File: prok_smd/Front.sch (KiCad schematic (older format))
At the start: 31 parts, among them CON1 microSD_Card, J12 Conn_01x05_Male, J13 Conn_01x04_Male, J14 Conn_01x04_Male, J5 TIME_CV, J6 CHANNEL_CV, J7 RESET_CV, J8 OUT, SW1 KS01BL

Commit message: :construction: Locked headers and added mousebites
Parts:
- removed J13, J14: Conn_01x04_Male, Connector_PinHeader_2.54mm:PinHeader_1x04_P2.54mm_Vertical, symbol Connector:Conn_01x04_Male
- added J15, J16, J17, J18: Conn_01x02_Male, Connector_PinHeader_2.54mm:PinHeader_1x02_P2.54mm_Vertical, symbol Connector:Conn_01x02_Male
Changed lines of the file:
@@
 L power:-12V #PWR?
 U 1 1 5D1D35EB
-P 2650 7050
+P 2650 7250
 AR Path="/5D1D35EB" Ref="#PWR?"  Part="1"
 AR Path="/5D2626DC/5D1D35EB" Ref="#PWR0142"  Part="1"
-F 0 "#PWR0142" H 2650 7150 50  0001 C CNN
-F 1 "-12V" H 2665 7223 50  0000 C CNN
-F 2 "" H 2650 7050 50  0001 C CNN
-F 3 "" H 2650 7050 50  0001 C CNN
-	1    2650 7050
+F 0 "#PWR0142" H 2650 7350 50  0001 C CNN
+F 1 "-12V" H 2665 7423 50  0000 C CNN
+F 2 "" H 2650 7250 50  0001 C CNN
+F 3 "" H 2650 7250 50  0001 C CNN
+	1    2650 7250
 	0    -1   -1   0
 $EndComp
@@
 L power:+5V #PWR?
 U 1 1 5D1D35FD
-P 2650 7250
+P 2650 7050
 AR Path="/5D1D35FD" Ref="#PWR?"  Part="1"
 AR Path="/5D2626DC/5D1D35FD" Ref="#PWR0145"  Part="1"
-F 0 "#PWR0145" H 2650 7100 50  0001 C CNN
-F 1 "+5V" V 2665 7378 50  0000 L CNN
-F 2 "" H 2650 7250 50  0001 C CNN
-F 3 "" H 2650 7250 50  0001 C CNN
-	1    2650 7250
+F 0 "#PWR0145" H 2650 6900 50  0001 C CNN
+F 1 "+5V" V 2665 7178 50  0000 L CNN
+F 2 "" H 2650 7050 50  0001 C CNN
+F 3 "" H 2650 7050 50  0001 C CNN
+	1    2650 7050
 	0    -1   -1   0
 $EndComp
@@
 	2650 7250 2750 7250
 $Comp
-L Connector:Conn_01x04_Male J13
-U 1 1 5D1D4B46
-P 4050 7050
-F 0 "J13" H 4156 7328 50  0000 C CNN
-F 1 "Conn_01x04_Male" H 4156 7237 50  0000 C CNN
-F 2 "Connector_PinHeader_2.54mm:PinHeader_1x04_P2.54mm_Vertical" H 4050 7050 50  0001 C CNN
-F 3 "~" H 4050 7050 50  0001 C CNN
-	1    4050 7050
-	1    0    0    -1
-$EndComp
-$Comp
-L Connector:Conn_01x04_Male J14
-U 1 1 5D1D4BBA
-P 4650 7150
-F 0 "J14" H 4623 7030 50  0000 R CNN
-F 1 "Conn_01x04_Male" H 4623 7121 50  0000 R CNN
-F 2 "Connector_PinHeader_2.54mm:PinHeader_1x04_P2.54mm_Vertical" H 4650 7150 50  0001 C CNN
-F 3 "~" H 4650 7150 50  0001 C CNN
-	1    4650 7150
-	-1   0    0    1
-$EndComp
-$Comp
 L Connector:Conn_01x05_Male J12
 U 1 1 5D1DA55A
@@
 	-1   0    0    -1
 $EndComp
+$Comp
+L Connector:Conn_01x02_Male J15
+U 1 1 5D21284E
+P 4050 6950
+F 0 "J15" H 4156 7128 50  0000 C CNN
+F 1 "Conn_01x02_Male" H 4156 7037 50  0000 C CNN
+F 2 "Connector_PinHeader_2.54mm:PinHeader_1x02_P2.54mm_Vertical" H 4050 6950 50  0001 C CNN
+F 3 "~" H 4050 6950 50  0001 C CNN
+	1    4050 6950
+	1    0    0    -1
+$EndComp
+$Comp
+L Connector:Conn_01x02_Male J16
+U 1 1 5D2128C0
+P 4050 7150
+F 0 "J16" H 4156 7328 50  0000 C CNN
+F 1 "Conn_01x02_Male" H 4156 7237 50  0000 C CNN
+F 2 "Connector_PinHeader_2.54mm:PinHeader_1x02_P2.54mm_Vertical" H 4050 7150 50  0001 C CNN
+F 3 "~" H 4050 7150 50  0001 C CNN
+	1    4050 7150
+	1    0    0    -1
+$EndComp
+$Comp
+L Connector:Conn_01x02_Male J17
+U 1 1 5D212916
+P 4650 7050
+F 0 "J17" H 4623 6930 50  0000 R CNN
+F 1 "Conn_01x02_Male" H 4623 7021 50  0000 R CNN
+F 2 "Connector_PinHeader_2.54mm:PinHeader_1x02_P2.54mm_Vertical" H 4650 7050 50  0001 C CNN
+F 3 "~" H 4650 7050 50  0001 C CNN
+	1    4650 7050
+	-1   0    0    1
+$EndComp
+$Comp
+L Connector:Conn_01x02_Male J18
+U 1 1 5D2129C8
+P 4650 7250
+F 0 "J18" H 4623 7130 50  0000 R CNN
+F 1 "Conn_01x02_Male" H 4623 7221 50  0000 R CNN
+F 2 "Connector_PinHeader_2.54mm:PinHeader_1x02_P2.54mm_Vertical" H 4650 7250 50  0001 C CNN
+F 3 "~" H 4650 7250 50  0001 C CNN
+	1    4650 7250
+	-1   0    0    1
+$EndComp
 $EndSCHEMATC

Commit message: :construction: first draft routing
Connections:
- wire segments 64 -> 68
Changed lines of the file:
@@
 	4350 7250 4450 7250
-Wire Wire Line
-	4450 7150 4250 7150
-Wire Wire Line
-	4250 7050 4450 7050
 Wire Wire Line
 	4450 6950 4350 6950
 Wire Wire Line
-	4350 6950 4350 7250
+	4350 6950 4350 7050
 Connection ~ 4350 6950
 Wire Wire Line
@@
 	-1   0    0    1
 $EndComp
+Wire Wire Line
+	4250 7050 4350 7050
+Connection ~ 4350 7050
+Wire Wire Line
+	4350 7050 4350 7150
+Wire Wire Line
+	4350 7050 4450 7050
+Wire Wire Line
+	4250 7150 4350 7150
+Connection ~ 4350 7150
+Wire Wire Line
+	4350 7150 4350 7250
+Wire Wire Line
+	4350 7150 4450 7150
 $EndSCHEMATC

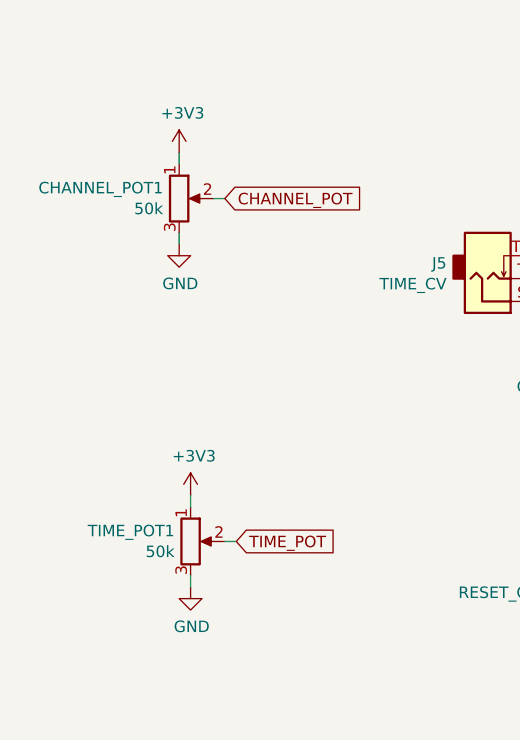
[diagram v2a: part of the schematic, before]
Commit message: :bug: fixed backwards pots
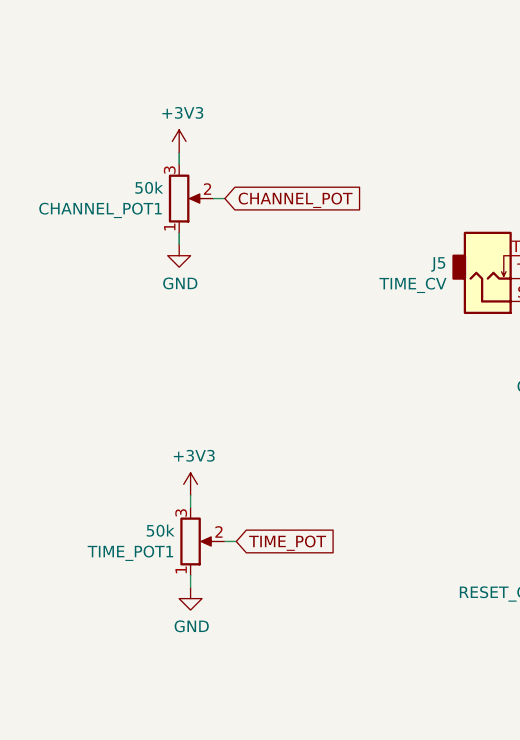
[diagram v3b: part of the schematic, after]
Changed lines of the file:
@@
 F 3 "~" H 1350 2750 50  0001 C CNN
 	1    1350 2750
-	1    0    0    -1
+	1    0    0    1
 $EndComp
 $Comp
@@
 F 3 "~" H 1400 4250 50  0001 C CNN
 	1    1400 4250
-	1    0    0    -1
+	1    0    0    1
 $EndComp
 $Comp

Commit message: :sparkles: Fixed switch led
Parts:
- removed D9: LED, symbol Device:LED
- removed SW1: KS01BL, prok_smd:KS01BL, symbol Switch:SW_SPST
- added SW1: SW_Push_LED, prok_smd:KS01BL, symbol Switch:SW_Push_LED
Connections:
- wire segments 68 -> 66
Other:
- moved on the sheet: R12
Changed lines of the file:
@@
 L Device:R R12
 U 1 1 5D27E545
-P 5550 1450
-F 0 "R12" H 5620 1496 50  0000 L CNN
-F 1 "27k" H 5620 1405 50  0000 L CNN
-F 2 "Resistor_SMD:R_0603_1608Metric" V 5480 1450 50  0001 C CNN
-F 3 "~" H 5550 1450 50  0001 C CNN
-	1    5550 1450
+P 5600 1900
+F 0 "R12" H 5670 1946 50  0000 L CNN
+F 1 "27k" H 5670 1855 50  0000 L CNN
+F 2 "Resistor_SMD:R_0603_1608Metric" V 5530 1900 50  0001 C CNN
+F 3 "~" H 5600 1900 50  0001 C CNN
+	1    5600 1900
 	1    0    0    -1
 $EndComp
@@
 L power:GND #PWR0126
 U 1 1 5D280887
-P 5550 1650
-F 0 "#PWR0126" H 5550 1400 50  0001 C CNN
-F 1 "GND" H 5555 1477 50  0000 C CNN
-F 2 "" H 5550 1650 50  0001 C CNN
-F 3 "" H 5550 1650 50  0001 C CNN
-	1    5550 1650
-	1    0    0    -1
-$EndComp
-Wire Wire Line
-	5550 1650 5550 1600
-Wire Wire Line
-	5550 1300 6000 1300
-$Comp
-L Switch:SW_SPST SW1
-U 1 1 5D280CD0
-P 5200 1300
-F 0 "SW1" H 5200 1535 50  0000 C CNN
-F 1 "KS01BL" H 5200 1444 50  0000 C CNN
-F 2 "prok_smd:KS01BL" H 5200 1300 50  0001 C CNN
-F 3 "" H 5200 1300 50  0001 C CNN
-	1    5200 1300
-	1    0    0    -1
-$EndComp
-Wire Wire Line
-	5400 1300 5550 1300
-Connection ~ 5550 1300
+P 5600 2100
+F 0 "#PWR0126" H 5600 1850 50  0001 C CNN
+F 1 "GND" H 5605 1927 50  0000 C CNN
+F 2 "" H 5600 2100 50  0001 C CNN
+F 3 "" H 5600 2100 50  0001 C CNN
+	1    5600 2100
+	1    0    0    -1
+$EndComp
+Wire Wire Line
+	5600 2100 5600 2050
+Wire Wire Line
+	5600 1750 6050 1750
 $Comp
 L power:+3V3 #PWR0127
 U 1 1 5D280FF6
-P 4950 1300
-F 0 "#PWR0127" H 4950 1150 50  0001 C CNN
-F 1 "+3V3" V 4965 1428 50  0000 L CNN
-F 2 "" H 4950 1300 50  0001 C CNN
-F 3 "" H 4950 1300 50  0001 C CNN
-	1    4950 1300
-	0    -1   -1   0
-$EndComp
-Wire Wire Line
-	4950 1300 5000 1300
-Text GLabel 6000 1300 2    50   Input ~ 0
+P 4850 1500
+F 0 "#PWR0127" H 4850 1350 50  0001 C CNN
+F 1 "+3V3" V 4865 1628 50  0000 L CNN
+F 2 "" H 4850 1500 50  0001 C CNN
+F 3 "" H 4850 1500 50  0001 C CNN
+	1    4850 1500
+	1    0    0    -1
+$EndComp
+Text GLabel 6050 1750 2    50   Input ~ 0
 RESET_SW
 $Comp
@@
 $EndComp
 $Comp
-L Device:R R17
-U 1 1 5D284B3C
-P 7050 4500
-F 0 "R17" V 7100 4350 50  0000 C CNN
-F 1 "1.5k" V 7050 4500 50  0000 C CNN
-F 2 "Resistor_SMD:R_0603_1608Metric" V 6980 4500 50  0001 C CNN
-F 3 "~" H 7050 4500 50  0001 C CNN
-	1    7050 4500
-	0    -1   -1   0
-$EndComp
-$Comp
 L Device:LED D5
 U 1 1 5D284BD7
@@
 	1    0    0    1
 $EndComp
-$Comp
-L Device:LED D9
-U 1 1 5D284F98
-P 7500 4500
-F 0 "D9" H 7800 4450 50  0000 C CNN
-F 1 "LED" H 7650 4450 50  0000 C CNN
-F 2 "" H 7500 4500 50  0001 C CNN
-F 3 "~" H 7500 4500 50  0001 C CNN
-	1    7500 4500
-	1    0    0    1
-$EndComp
-Wire Wire Line
-	7350 4500 7200 4500
 Wire Wire Line
 	7200 4400 7350 4400
@@
 	6900 4300 6900 4400
 Connection ~ 6900 4400
-Wire Wire Line
-	6900 4400 6900 4500
-Connection ~ 6900 4500
-Wire Wire Line
-	6900 4500 6900 4650
 $Comp
 L power:GND #PWR0132
@@
 Text GLabel 7900 4400 2    50   Input ~ 0
 LED_4
-Text GLabel 7900 4500 2    50   Input ~ 0
-LED_RESET
-Wire Wire Line
-	7900 4500 7650 4500
 Wire Wire Line
 	7650 4400 7900 4400
@@
 Wire Wire Line
 	4350 7150 4450 7150
+Wire Wire Line
+	6900 4400 6900 4650
+$Comp
+L Device:R R17
+U 1 1 5D2545C9
+P 4850 1850
+F 0 "R17" V 4900 1700 50  0000 C CNN
+F 1 "1.5k" V 4850 1850 50  0000 C CNN
+F 2 "Resistor_SMD:R_0603_1608Metric" V 4780 1850 50  0001 C CNN
+F 3 "~" H 4850 1850 50  0001 C CNN
+	1    4850 1850
+	0    -1   -1   0
+$EndComp
+Text GLabel 5400 1850 3    50   Input ~ 0
+LED_RESET
+$Comp
+L power:GND #PWR0147
+U 1 1 5D255C36
+P 4700 1850
+F 0 "#PWR0147" H 4700 1600 50  0001 C CNN
+F 1 "GND" H 4705 1677 50  0000 C CNN
+F 2 "" H 4700 1850 50  0001 C CNN
+F 3 "" H 4700 1850 50  0001 C CNN
+	1    4700 1850
+	1    0    0    -1
+$EndComp
+$Comp
+L Switch:SW_Push_LED SW1
+U 1 1 5D255D2D
+P 5200 1850
+F 0 "SW1" H 5200 2235 50  0000 C CNN
+F 1 "SW_Push_LED" H 5200 2144 50  0000 C CNN
+F 2 "prok_smd:KS01BL" H 5200 2150 50  0001 C CNN
+F 3 "" H 5200 2150 50  0001 C CNN
+	1    5200 1850
+	1    0    0    -1
+$EndComp
+Wire Wire Line
+	5400 1750 5600 1750
+Connection ~ 5600 1750
+Wire Wire Line
+	4850 1500 4850 1750
+Wire Wire Line
+	4850 1750 5000 1750
 $EndSCHEMATC

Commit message: :sparkles: :construction: first draft v2 board
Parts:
- removed J15, J16, J17, J18: Conn_01x02_Male, Connector_PinHeader_2.54mm:PinHeader_1x02_P2.54mm_Vertical, symbol Connector:Conn_01x02_Male
- added J17: Conn_01x03_Male, Connector_PinHeader_2.54mm:PinHeader_1x03_P2.54mm_Vertical, symbol Connector:Conn_01x03_Male
- renumbered CHANNEL_POT1 to CHANNEL1, TIME_POT1 to TIME1
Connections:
- net GND: now also J17.1 (Pin_1), J17.2 (Pin_2), J17.3 (Pin_3)
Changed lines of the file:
@@
 RESET_SW
 $Comp
-L Device:R_POT CHANNEL_POT1
+L Device:R_POT CHANNEL1
 U 1 1 5D281D3E
 P 1350 2750
-F 0 "CHANNEL_POT1" H 1280 2796 50  0000 R CNN
+F 0 "CHANNEL1" H 1280 2796 50  0000 R CNN
 F 1 "50k" H 1280 2705 50  0000 R CNN
 F 2 "4ms-footprints:POT-9MM-ALPHA" H 1350 2750 50  0001 C CNN
@@
 	1550 2750 1500 2750
 $Comp
-L Device:R_POT TIME_POT1
+L Device:R_POT TIME1
 U 1 1 5D282FDC
 P 1400 4250
-F 0 "TIME_POT1" H 1330 4296 50  0000 R CNN
+F 0 "TIME1" H 1330 4296 50  0000 R CNN
 F 1 "50k" H 1330 4205 50  0000 R CNN
 F 2 "4ms-footprints:POT-9MM-ALPHA" H 1400 4250 50  0001 C CNN
@@
 $EndComp
 Wire Wire Line
-	4250 7250 4350 7250
-Connection ~ 4350 7250
-Wire Wire Line
-	4350 7250 4450 7250
-Wire Wire Line
 	4450 6950 4350 6950
 Wire Wire Line
 	4350 6950 4350 7050
 Connection ~ 4350 6950
-Wire Wire Line
-	4350 6950 4250 6950
 $Comp
 L power:-12V #PWR?
@@
 	-1   0    0    -1
 $EndComp
-$Comp
-L Connector:Conn_01x02_Male J15
-U 1 1 5D21284E
-P 4050 6950
-F 0 "J15" H 4156 7128 50  0000 C CNN
-F 1 "Conn_01x02_Male" H 4156 7037 50  0000 C CNN
-F 2 "Connector_PinHeader_2.54mm:PinHeader_1x02_P2.54mm_Vertical" H 4050 6950 50  0001 C CNN
-F 3 "~" H 4050 6950 50  0001 C CNN
-	1    4050 6950
-	1    0    0    -1
-$EndComp
-$Comp
-L Connector:Conn_01x02_Male J16
-U 1 1 5D2128C0
-P 4050 7150
-F 0 "J16" H 4156 7328 50  0000 C CNN
-F 1 "Conn_01x02_Male" H 4156 7237 50  0000 C CNN
-F 2 "Connector_PinHeader_2.54mm:PinHeader_1x02_P2.54mm_Vertical" H 4050 7150 50  0001 C CNN
-F 3 "~" H 4050 7150 50  0001 C CNN
-	1    4050 7150
-	1    0    0    -1
-$EndComp
-$Comp
-L Connector:Conn_01x02_Male J17
-U 1 1 5D212916
-P 4650 7050
-F 0 "J17" H 4623 6930 50  0000 R CNN
-F 1 "Conn_01x02_Male" H 4623 7021 50  0000 R CNN
-F 2 "Connector_PinHeader_2.54mm:PinHeader_1x02_P2.54mm_Vertical" H 4650 7050 50  0001 C CNN
-F 3 "~" H 4650 7050 50  0001 C CNN
-	1    4650 7050
-	-1   0    0    1
-$EndComp
-$Comp
-L Connector:Conn_01x02_Male J18
-U 1 1 5D2129C8
-P 4650 7250
-F 0 "J18" H 4623 7130 50  0000 R CNN
-F 1 "Conn_01x02_Male" H 4623 7221 50  0000 R CNN
-F 2 "Connector_PinHeader_2.54mm:PinHeader_1x02_P2.54mm_Vertical" H 4650 7250 50  0001 C CNN
-F 3 "~" H 4650 7250 50  0001 C CNN
-	1    4650 7250
-	-1   0    0    1
-$EndComp
-Wire Wire Line
-	4250 7050 4350 7050
 Connection ~ 4350 7050
 Wire Wire Line
-	4350 7050 4350 7150
-Wire Wire Line
 	4350 7050 4450 7050
-Wire Wire Line
-	4250 7150 4350 7150
-Connection ~ 4350 7150
-Wire Wire Line
-	4350 7150 4350 7250
-Wire Wire Line
-	4350 7150 4450 7150
 Wire Wire Line
 	6900 4400 6900 4650
@@
 Wire Wire Line
 	4850 1750 5000 1750
+$Comp
+L Connector:Conn_01x03_Male J17
+U 1 1 5D1D7379
+P 4650 6950
+F 0 "J17" H 4623 6880 50  0000 R CNN
+F 1 "Conn_01x03_Male" H 4623 6971 50  0000 R CNN
+F 2 "Connector_PinHeader_2.54mm:PinHeader_1x03_P2.54mm_Vertical" H 4650 6950 50  0001 C CNN
+F 3 "~" H 4650 6950 50  0001 C CNN
+	1    4650 6950
+	-1   0    0    1
+$EndComp
+Wire Wire Line
+	4350 6950 4350 6850
+Wire Wire Line
+	4350 6850 4450 6850
+Wire Wire Line
+	4350 7050 4350 7250
 $EndSCHEMATC

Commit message: :recycle: redid power pcb single
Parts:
- J17: value Conn_01x03_Male -> Conn_01x05_Male; footprint Connector_PinHeader_2.54mm:PinHeader_1x03_P2.54mm_Vertical -> Connector_PinHeader_2.54mm:PinHeader_1x05_P2.54mm_Vertical; symbol Connector:Conn_01x03_Male -> Connector:Conn_01x05_Male
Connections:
- net GND: now also J17.4 (Pin_4), J17.5 (Pin_5)
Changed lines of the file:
@@
 EESchema Schematic File Version 4
-LIBS:prok_smd-cache
-EELAYER 26 0
+EELAYER 30 0
 EELAYER END
 $Descr A4 11693 8268
@@
 	4850 1750 5000 1750
 $Comp
-L Connector:Conn_01x03_Male J17
+L Connector:Conn_01x05_Male J17
 U 1 1 5D1D7379
 P 4650 6950
 F 0 "J17" H 4623 6880 50  0000 R CNN
-F 1 "Conn_01x03_Male" H 4623 6971 50  0000 R CNN
-F 2 "Connector_PinHeader_2.54mm:PinHeader_1x03_P2.54mm_Vertical" H 4650 6950 50  0001 C CNN
+F 1 "Conn_01x05_Male" H 4623 6971 50  0000 R CNN
+F 2 "Connector_PinHeader_2.54mm:PinHeader_1x05_P2.54mm_Vertical" H 4650 6950 50  0001 C CNN
 F 3 "~" H 4650 6950 50  0001 C CNN
 	1    4650 6950
@@
 	4350 6850 4450 6850
 Wire Wire Line
-	4350 7050 4350 7250
+	4350 7050 4350 7150
+Wire Wire Line
+	4450 6750 4350 6750
+Wire Wire Line
+	4350 6750 4350 6850
+Connection ~ 4350 6850
+Wire Wire Line
+	4450 7150 4350 7150
+Connection ~ 4350 7150
+Wire Wire Line
+	4350 7150 4350 7250
 $EndSCHEMATC

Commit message: :recycle: rerouted all pcb
same


same
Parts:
- renumbered CHANNEL1 to X1, TIME1 to Y1
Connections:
- net GND: no longer J12.2 (Pin_2), J12.4 (Pin_4)
- no-connect marks 2 -> 4
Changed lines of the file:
@@
 RESET_SW
 $Comp
-L Device:R_POT CHANNEL1
+L Device:R_POT X1
 U 1 1 5D281D3E
 P 1350 2750
-F 0 "CHANNEL1" H 1280 2796 50  0000 R CNN
+F 0 "X1" H 1280 2796 50  0000 R CNN
 F 1 "50k" H 1280 2705 50  0000 R CNN
 F 2 "4ms-footprints:POT-9MM-ALPHA" H 1350 2750 50  0001 C CNN
@@
 	1550 2750 1500 2750
 $Comp
-L Device:R_POT TIME1
+L Device:R_POT Y1
 U 1 1 5D282FDC
 P 1400 4250
-F 0 "TIME1" H 1330 4296 50  0000 R CNN
+F 0 "Y1" H 1330 4296 50  0000 R CNN
 F 1 "50k" H 1330 4205 50  0000 R CNN
 F 2 "4ms-footprints:POT-9MM-ALPHA" H 1400 4250 50  0001 C CNN
@@
 $EndComp
 $Comp
-L power:GND #PWR?
-U 1 1 5D1D35F1
-P 2650 7150
-AR Path="/5D1D35F1" Ref="#PWR?"  Part="1"
-AR Path="/5D2626DC/5D1D35F1" Ref="#PWR0143"  Part="1"
-F 0 "#PWR0143" H 2650 6900 50  0001 C CNN
-F 1 "GND" V 2655 7022 50  0000 R CNN
-F 2 "" H 2650 7150 50  0001 C CNN
-F 3 "" H 2650 7150 50  0001 C CNN
-	1    2650 7150
-	0    1    1    0
-$EndComp
-$Comp
-L power:GND #PWR?
-U 1 1 5D1D35F7
-P 2650 6950
-AR Path="/5D1D35F7" Ref="#PWR?"  Part="1"
-AR Path="/5D2626DC/5D1D35F7" Ref="#PWR0144"  Part="1"
-F 0 "#PWR0144" H 2650 6700 50  0001 C CNN
-F 1 "GND" V 2655 6822 50  0000 R CNN
-F 2 "" H 2650 6950 50  0001 C CNN
-F 3 "" H 2650 6950 50  0001 C CNN
-	1    2650 6950
-	0    1    1    0
-$EndComp
-$Comp
 L power:+5V #PWR?
 U 1 1 5D1D35FD
@@
 	2650 6850 2750 6850
 Wire Wire Line
-	2750 6950 2650 6950
-Wire Wire Line
 	2650 7050 2750 7050
-Wire Wire Line
-	2750 7150 2650 7150
 Wire Wire Line
 	2650 7250 2750 7250
@@
 Wire Wire Line
 	4350 7150 4350 7250
+NoConn ~ 2750 6950
+NoConn ~ 2750 7150
 $EndSCHEMATC
